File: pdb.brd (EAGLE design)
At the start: 50 x 108 mm, 38 parts, among them Q1 20MHz, Q2 IRFR5305PBF, Q3 IRFR5305PBF, U1 TSR_1-2433, U2 LTC2946CMSPBF, U3 LTC2946CMSPBF, U4 LTC2946CMSPBF, U5 ATMEGA48-20AU, U6 TXB0104, U7 AT30TS74SS8M

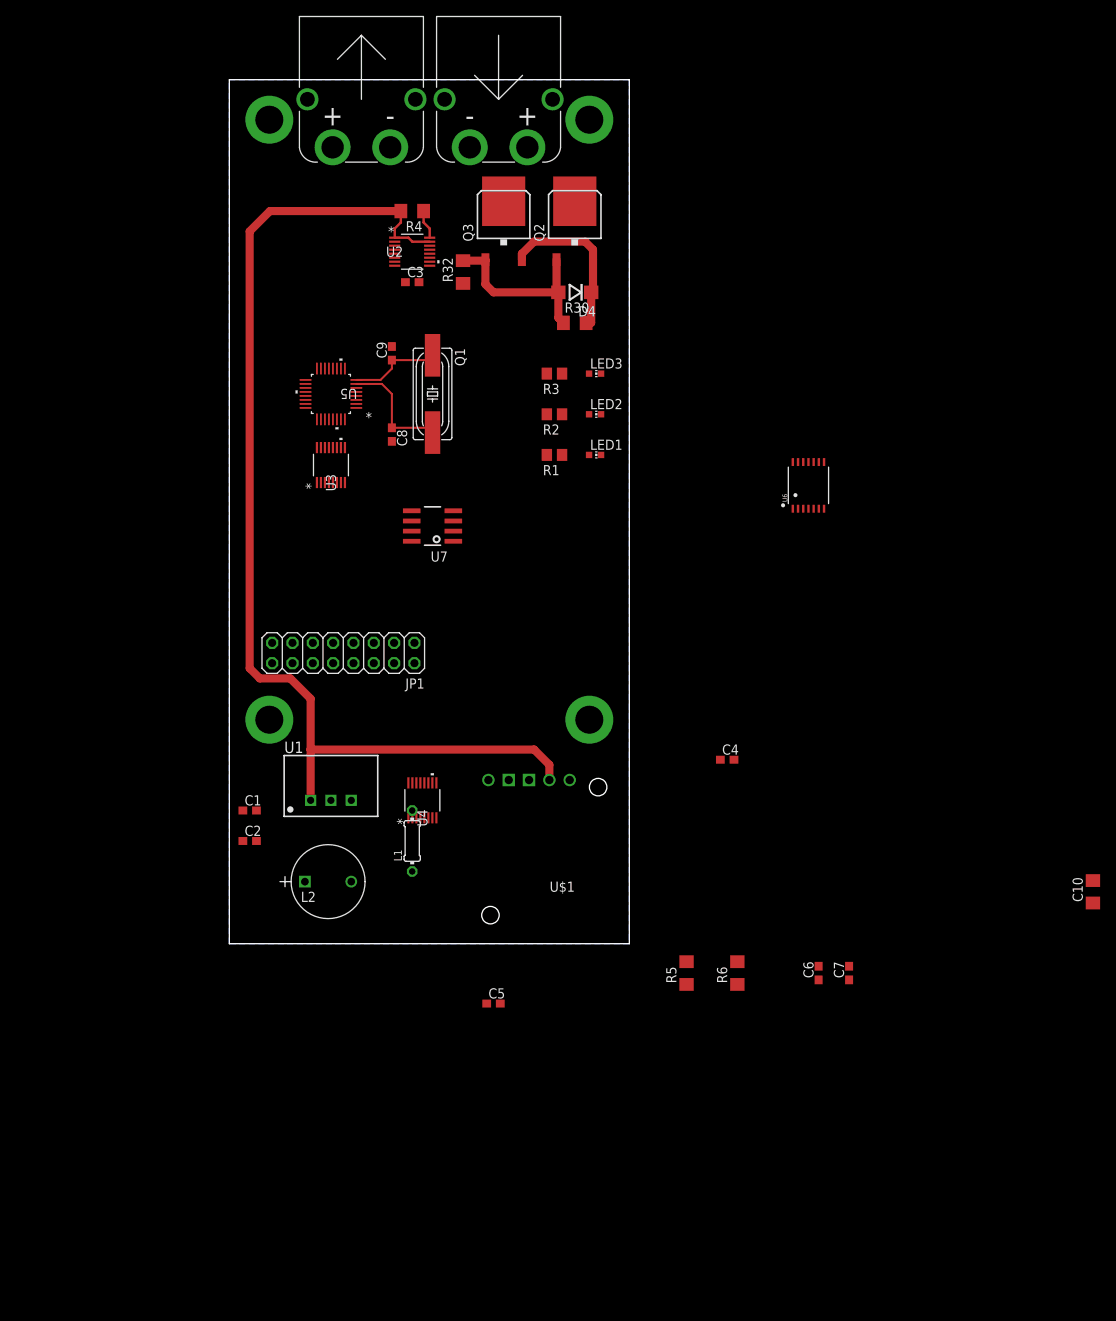
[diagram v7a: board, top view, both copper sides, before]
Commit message: 5v nearly completely connected
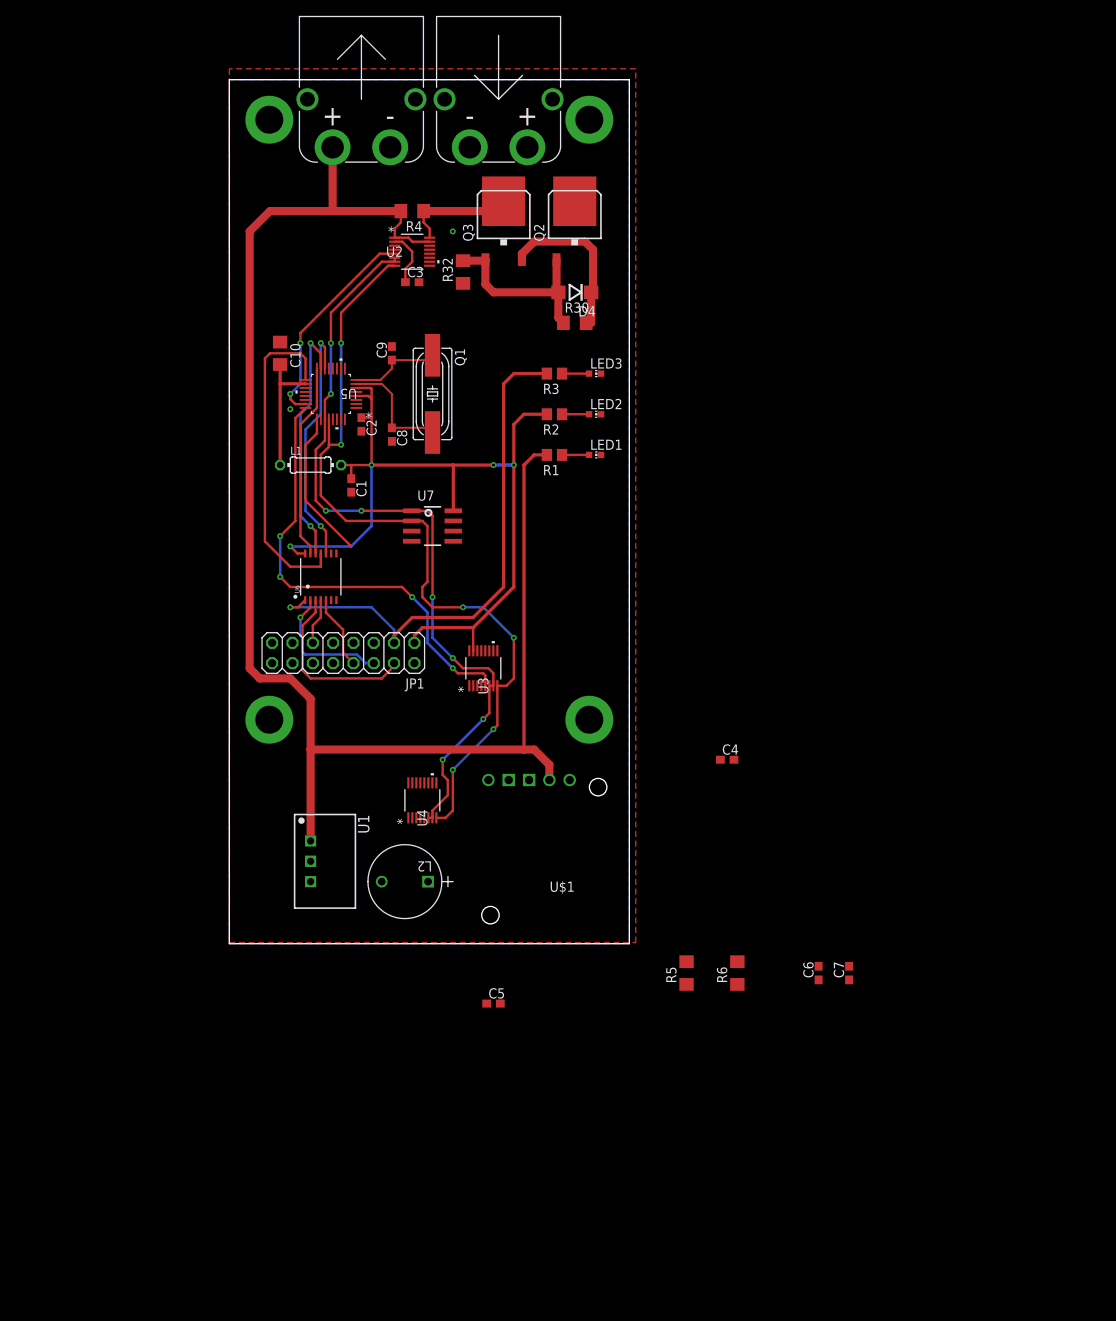
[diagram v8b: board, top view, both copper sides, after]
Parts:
- moved C10 121.9 mm to (6.35, 50.8), turned to 270 degrees
- moved U6 62.0 mm to (11.4, 22.9)
- moved C2 53.9 mm to (16.5, 41.9), turned to 270 degrees
- moved L1 48.7 mm to (10.2, 36.8), turned to 0 degrees
- moved C1 42.6 mm to (15.2, 34.3), turned to 270 degrees
- moved U3 31.8 mm to (31.8, 11.4)
- moved U1 8.03 mm to (10.2, -12.7), turned to 270 degrees
- moved L2 3.81 mm to (19.1, -15.2), turned to 180 degrees
- turned U7 to 270 degrees
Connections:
- removed net ADIN_3V3: U4.13
- removed net ADIN_5V: U3.13
- removed net ADIN_V+: U2.13
- removed net AVCC: U5.18
- removed net CLKIN_3V3: U4.9
- removed net CLKIN_5V: U3.9
- removed net CLKIN_V+: U2.9
- removed net CLKOUT_3V3: U4.10
- removed net CLKOUT_5V: U3.10
- removed net CLKOUT_V+: U2.10
- removed net N$10: U5.20
- removed net N$11: U7.3
- removed net N$13: U7.5
- removed net N$14: U7.6
- removed net N$15: U5.26
- removed net N$16: U7.7
- removed net N$19: U5.30
- removed net N$20: U5.31
- removed net N$21: U5.32
- removed net N$22: U5.12
- removed net N$23: U5.13
- removed net N$29: U5.1
- removed net N$30: U5.2
- removed net N$31: U5.9
- removed net N$32: U5.10
- removed net N$33: U5.11
- removed net N$8: U5.19
- removed net N$9: U5.22
- removed net SCL_5V: U7.2
- removed net SDA_5V: U7.1
- net N$88: now also U5.18
- net SCL: now also U7.2
- net SDA: now also U7.1
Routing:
- net +5V: track 0.00 -> 108.6 mm, vias 0 -> 4
- net SCL: track 0.00 -> 102.6 mm, vias 0 -> 6
- net SDA: track 0.00 -> 98.0 mm, vias 0 -> 8
- net +3V3: track 0.00 -> 66.4 mm, vias 0 -> 1
- net !ALERT_5V: track 0.00 -> 56.7 mm, vias 0 -> 4
- net V+: track 137.2 -> 189.2 mm
- net SCK_5V: track 0.00 -> 41.1 mm
- net SS_5V: track 0.00 -> 31.5 mm, vias 0 -> 2
- net MOSI_5V: track 0.00 -> 31.3 mm, vias 0 -> 2
- net !ALERT_V+: track 0.00 -> 26.9 mm, vias 0 -> 2
- net MISO_5V: track 0.00 -> 24.5 mm
- net EXT_SPI_MISO: track 0.00 -> 22.3 mm
- net !ALERT_3V3: track 0.00 -> 18.8 mm
- net EXT_SPI_MOSI: track 0.00 -> 16.6 mm, vias 0 -> 1
- net N$88: track 0.00 -> 15.8 mm
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- added copper zone on layer 1, net GND
